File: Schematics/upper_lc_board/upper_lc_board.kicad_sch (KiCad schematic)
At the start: 0 parts

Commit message: update power circuitry with new backplane symbol
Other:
- added sheet Untitled Sheet (../ESP32_breakout/ESP_breakout.kicad_sch)
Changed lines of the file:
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@@
 		(company "Queen's Rocket Engineering Team")
+	)
+	(sheet
+		(at 25.4 25.4)
+		(size 54.61 33.02)
+		(fields_autoplaced yes)
+		(stroke
+			(width 0.1524)
+			(type solid)
+		)
+		(fill
+			(color 0 0 0 0.0000)
+		)
+		(property "Sheetname" "Untitled Sheet"
+			(at 25.4 24.6884 0)
+			(effects
+				(font
+					(size 1.27 1.27)
+				)
+				(justify left bottom)
+			)
+		)
+		(property "Sheetfile" "../ESP32_breakout/ESP_breakout.kicad_sch"
+			(at 25.4 59.0046 0)
+			(effects
+				(font
+					(size 1.27 1.27)
+				)
+				(justify left top)
+			)
+		)
+		(instances
+			(project "upper_lc_board"
+				(path "/9b1a1d2a-fad7-4f10-83f3-1f83e9656c75"
+					(page "2")
+				)
+			)
+		)
 	)
 	(sheet_instances

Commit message: add hiearchical sheets in main board file
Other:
- sheet Untitled Sheet renamed ESP Breakout Cirucitry
- added sheet Power Circuitry (power_module/power_module.kicad_sch)
- added sheet Sensor Circuitry (sensor_module/sensor_module.kicad_sch)
- added sheet Solenoid Driver Circuitry (solenoid_module/solenoid_module.kicad_sch)
- sheet ESP Breakout Cirucitry: file ../ESP32_breakout/ESP_breakout.kicad_sch -> ESP_breakout_module/ESP_breakout_module.kicad_sch
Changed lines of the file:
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@@
 	)
 	(sheet
-		(at 25.4 25.4)
+		(at 72.39 102.87)
 		(size 54.61 33.02)
 		(fields_autoplaced yes)
@@
 			(color 0 0 0 0.0000)
 		)
-		(property "Sheetname" "Untitled Sheet"
-			(at 25.4 24.6884 0)
+		(property "Sheetname" "Sensor Circuitry"
+			(at 72.39 102.1584 0)
 			(effects
 				(font
@@
 			)
 		)
-		(property "Sheetfile" "../ESP32_breakout/ESP_breakout.kicad_sch"
-			(at 25.4 59.0046 0)
+		(property "Sheetfile" "sensor_module/sensor_module.kicad_sch"
+			(at 72.39 136.4746 0)
+			(effects
+				(font
+					(size 1.27 1.27)
+				)
+				(justify left top)
+			)
+		)
+		(instances
+			(project "upper_lc_board"
+				(path "/9b1a1d2a-fad7-4f10-83f3-1f83e9656c75"
+					(page "4")
+				)
+			)
+		)
+	)
+	(sheet
+		(at 71.12 44.45)
+		(size 54.61 33.02)
+		(fields_autoplaced yes)
+		(stroke
+			(width 0.1524)
+			(type solid)
+		)
+		(fill
+			(color 0 0 0 0.0000)
+		)
+		(property "Sheetname" "ESP Breakout Cirucitry"
+			(at 71.12 43.7384 0)
+			(effects
+				(font
+					(size 1.27 1.27)
+				)
+				(justify left bottom)
+			)
+		)
+		(property "Sheetfile" "ESP_breakout_module/ESP_breakout_module.kicad_sch"
+			(at 71.12 78.0546 0)
 			(effects
 				(font
@@
 				)
 			)
+		)
+	)
+	(sheet
+		(at 153.67 44.45)
+		(size 54.61 33.02)
+		(fields_autoplaced yes)
+		(stroke
+			(width 0.1524)
+			(type solid)
+		)
+		(fill
+			(color 0 0 0 0.0000)
+		)
+		(property "Sheetname" "Power Circuitry"
+			(at 153.67 43.7384 0)
+			(effects
+				(font
+					(size 1.27 1.27)
+				)
+				(justify left bottom)
+			)
+		)
+		(property "Sheetfile" "power_module/power_module.kicad_sch"
+			(at 153.67 78.0546 0)
+			(effects
+				(font
+					(size 1.27 1.27)
+				)
+				(justify left top)
+			)
+		)
+		(instances
+			(project "upper_lc_board"
+				(path "/9b1a1d2a-fad7-4f10-83f3-1f83e9656c75"
+					(page "3")
+				)
+			)
+		)
+	)
+	(sheet
+		(at 154.94 102.87)
+		(size 54.61 33.02)
+		(fields_autoplaced yes)
+		(stroke
+			(width 0.1524)
+			(type solid)
+		)
+		(fill
+			(color 0 0 0 0.0000)
+		)
+		(property "Sheetname" "Solenoid Driver Circuitry"
+			(at 154.94 102.1584 0)
+			(effects
+				(font
+					(size 1.27 1.27)
+				)
+				(justify left bottom)
+			)
+		)
+		(property "Sheetfile" "solenoid_module/solenoid_module.kicad_sch"
+			(at 154.94 136.4746 0)
+			(effects
+				(font
+					(size 1.27 1.27)
+				)
+				(justify left top)
+			)
+		)
+		(instances
+			(project "upper_lc_board"
+				(path "/9b1a1d2a-fad7-4f10-83f3-1f83e9656c75"
+					(page "5")
+				)
+			)

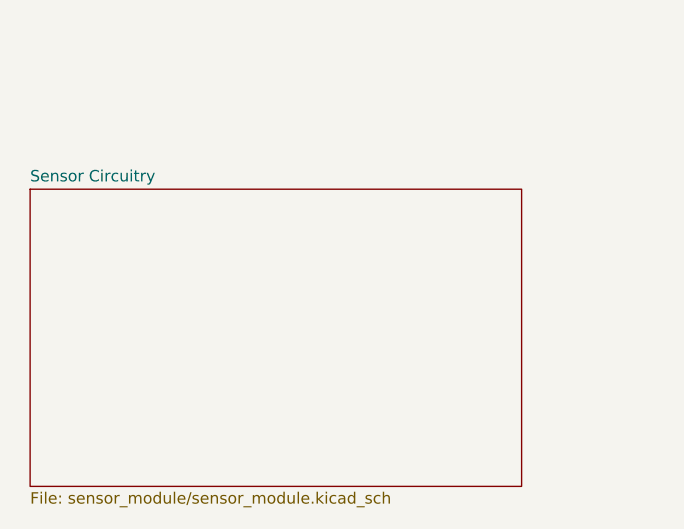
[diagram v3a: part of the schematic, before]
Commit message: start redesigning ADC circuitry, organize schematic files. adding OPAMPS for buffered voltage divider on HALL & on PTs. layout to be adjusted after.
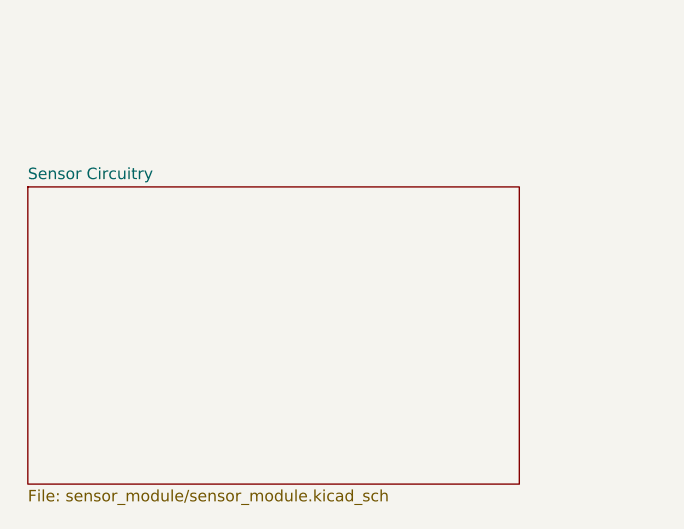
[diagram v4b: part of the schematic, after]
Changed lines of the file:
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@@
 	)
 	(sheet
-		(at 72.39 102.87)
+		(at 72.136 102.616)
 		(size 54.61 33.02)
 		(fields_autoplaced yes)
@@
 		)
 		(property "Sheetname" "Sensor Circuitry"
-			(at 72.39 102.1584 0)
+			(at 72.136 101.9044 0)
 			(effects
 				(font
@@
 		)
 		(property "Sheetfile" "sensor_module/sensor_module.kicad_sch"
-			(at 72.39 136.4746 0)
+			(at 72.136 136.2206 0)
 			(effects
 				(font

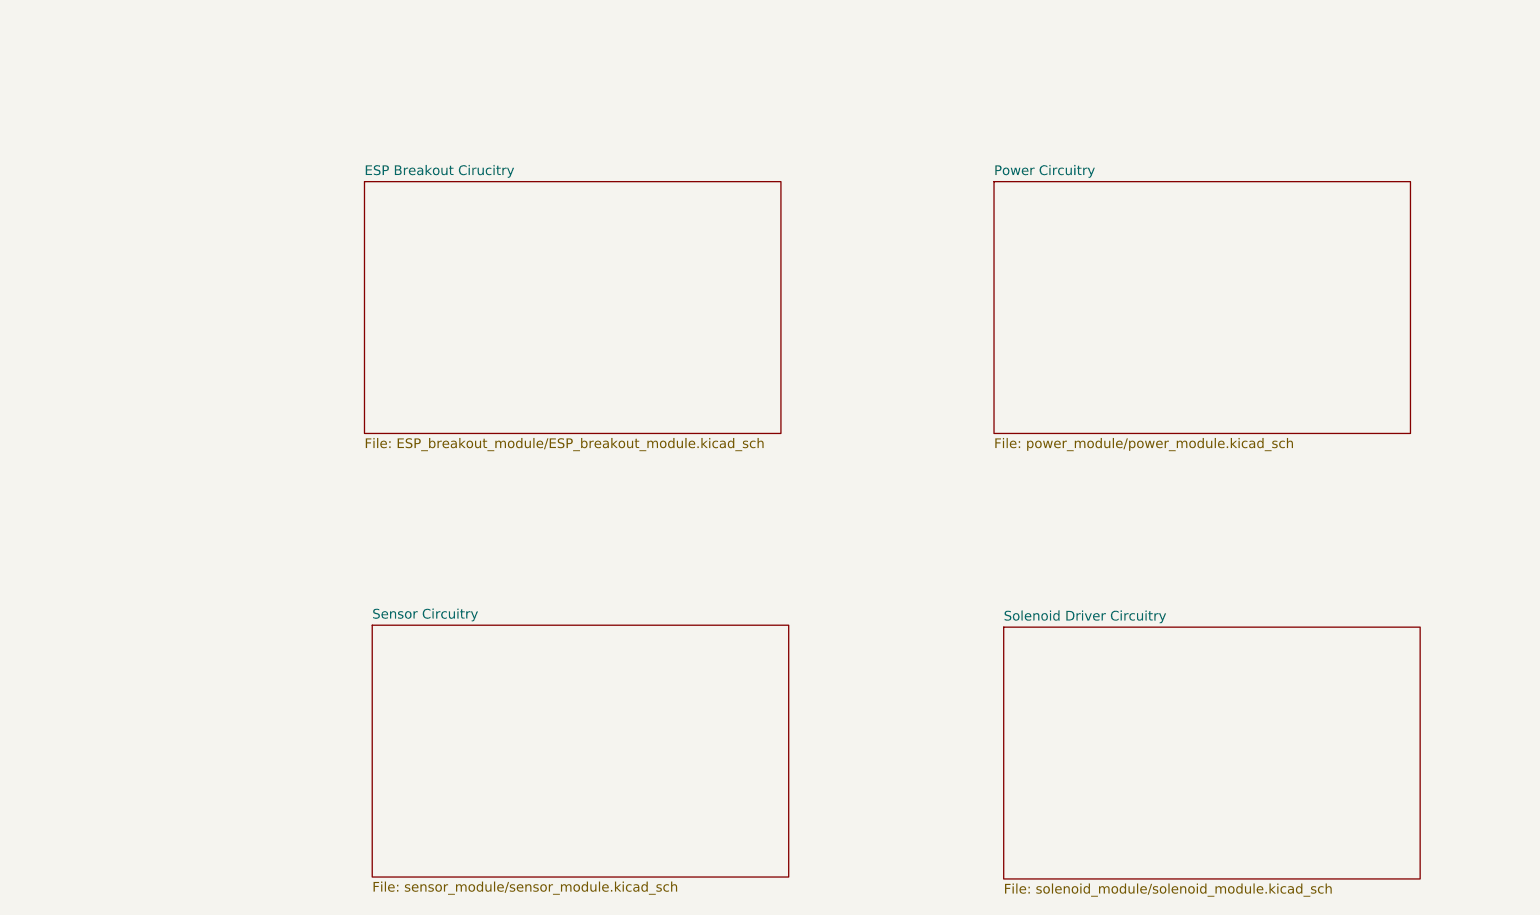
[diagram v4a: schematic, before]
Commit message: add hierarchy sheet blocks for valve, TC & PT circuitry.
confirmed that nets are consistent with layout, no problems.
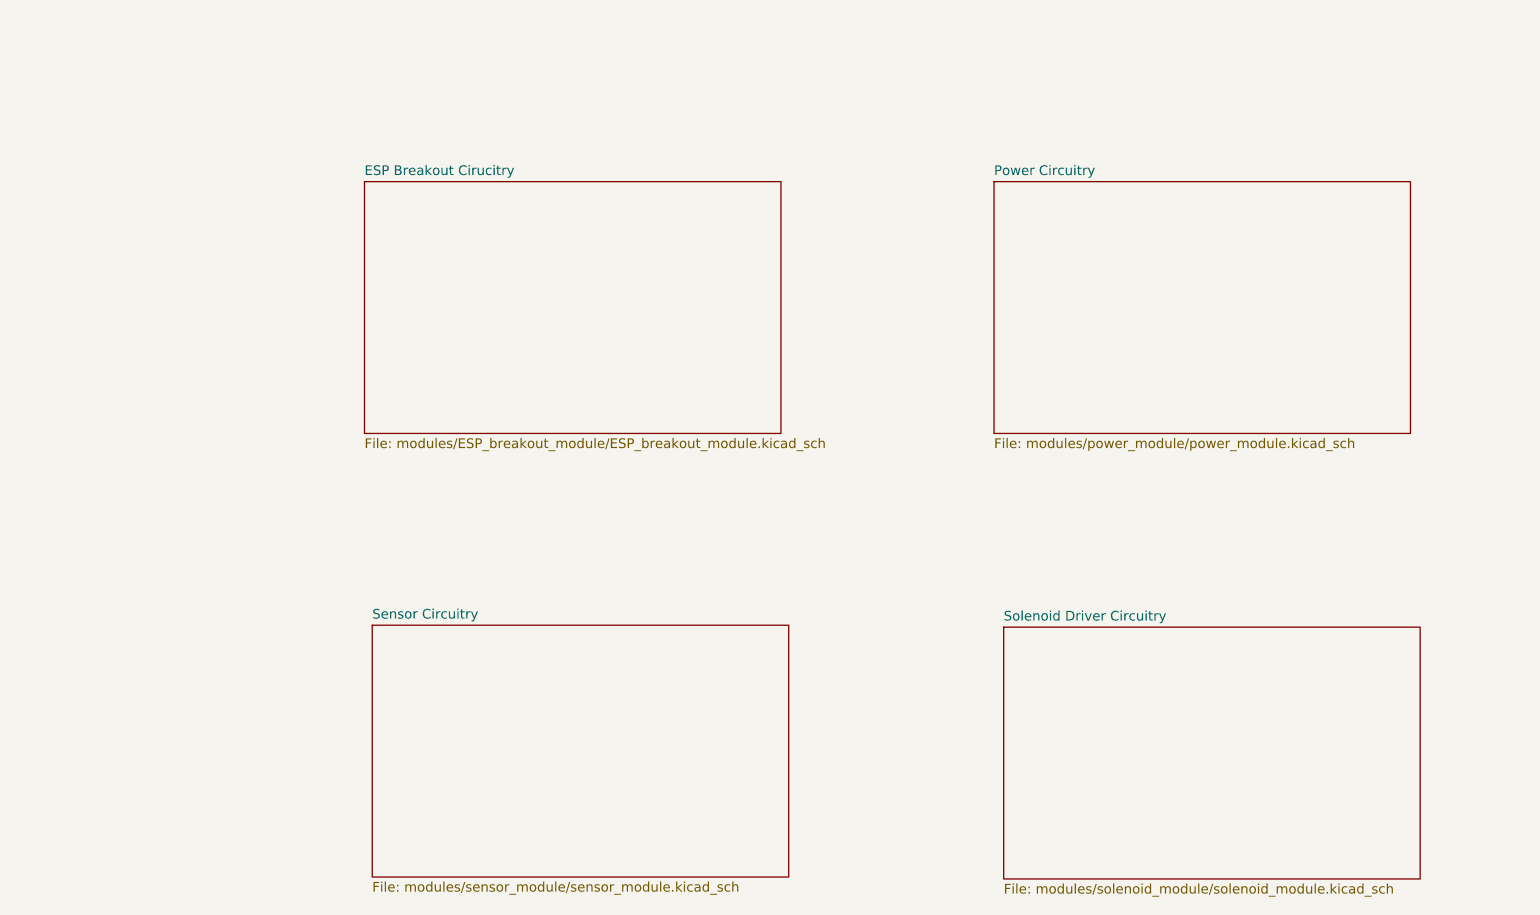
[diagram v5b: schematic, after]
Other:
- sheet ESP Breakout Cirucitry: file ESP_breakout_module/ESP_breakout_module.kicad_sch -> modules/ESP_breakout_module/ESP_breakout_module.kicad_sch
- sheet Power Circuitry: file power_module/power_module.kicad_sch -> modules/power_module/power_module.kicad_sch
- sheet Sensor Circuitry: file sensor_module/sensor_module.kicad_sch -> modules/sensor_module/sensor_module.kicad_sch
- sheet Solenoid Driver Circuitry: file solenoid_module/solenoid_module.kicad_sch -> modules/solenoid_module/solenoid_module.kicad_sch
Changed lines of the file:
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@@
 			)
 		)
-		(property "Sheetfile" "sensor_module/sensor_module.kicad_sch"
+		(property "Sheetfile" "modules/sensor_module/sensor_module.kicad_sch"
 			(at 72.136 136.2206 0)
 			(effects
@@
 			)
 		)
-		(property "Sheetfile" "ESP_breakout_module/ESP_breakout_module.kicad_sch"
+		(property "Sheetfile" "modules/ESP_breakout_module/ESP_breakout_module.kicad_sch"
 			(at 71.12 78.0546 0)
 			(effects
@@
 			)
 		)
-		(property "Sheetfile" "power_module/power_module.kicad_sch"
+		(property "Sheetfile" "modules/power_module/power_module.kicad_sch"
 			(at 153.67 78.0546 0)
 			(effects
@@
 			)
 		)
-		(property "Sheetfile" "solenoid_module/solenoid_module.kicad_sch"
+		(property "Sheetfile" "modules/solenoid_module/solenoid_module.kicad_sch"
 			(at 154.94 136.4746 0)
 			(effects
